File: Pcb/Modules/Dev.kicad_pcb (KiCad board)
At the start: 2 copper layers, 38.1 x 38.1 mm, 9 parts, among them J1 JACK_STEREO, J2 JACK_RJ45, P1 CONN_02X04, P2 CONN_02X04, Q1 BSS138P, U1 11AA160, X1 HOLE, X2 HOLE

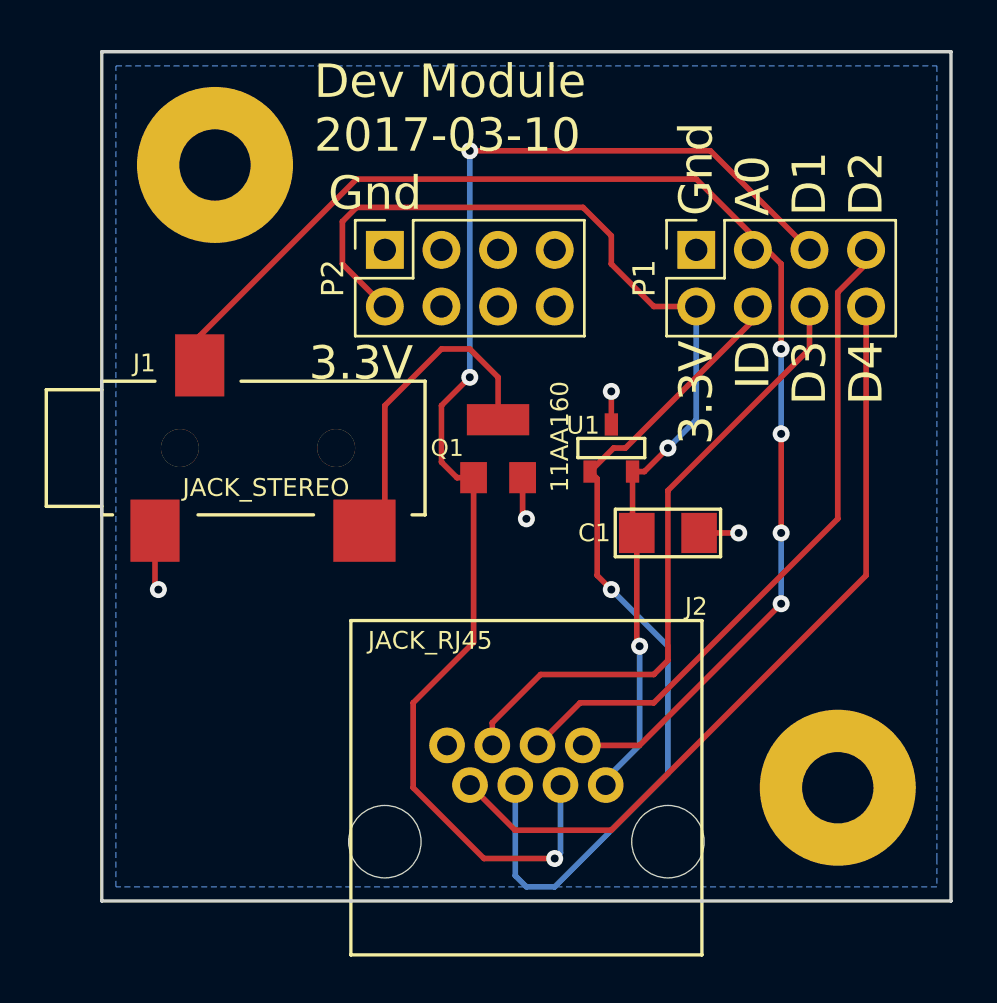
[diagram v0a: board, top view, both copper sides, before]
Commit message: Rework dev board layout so both parts are on same side of the case
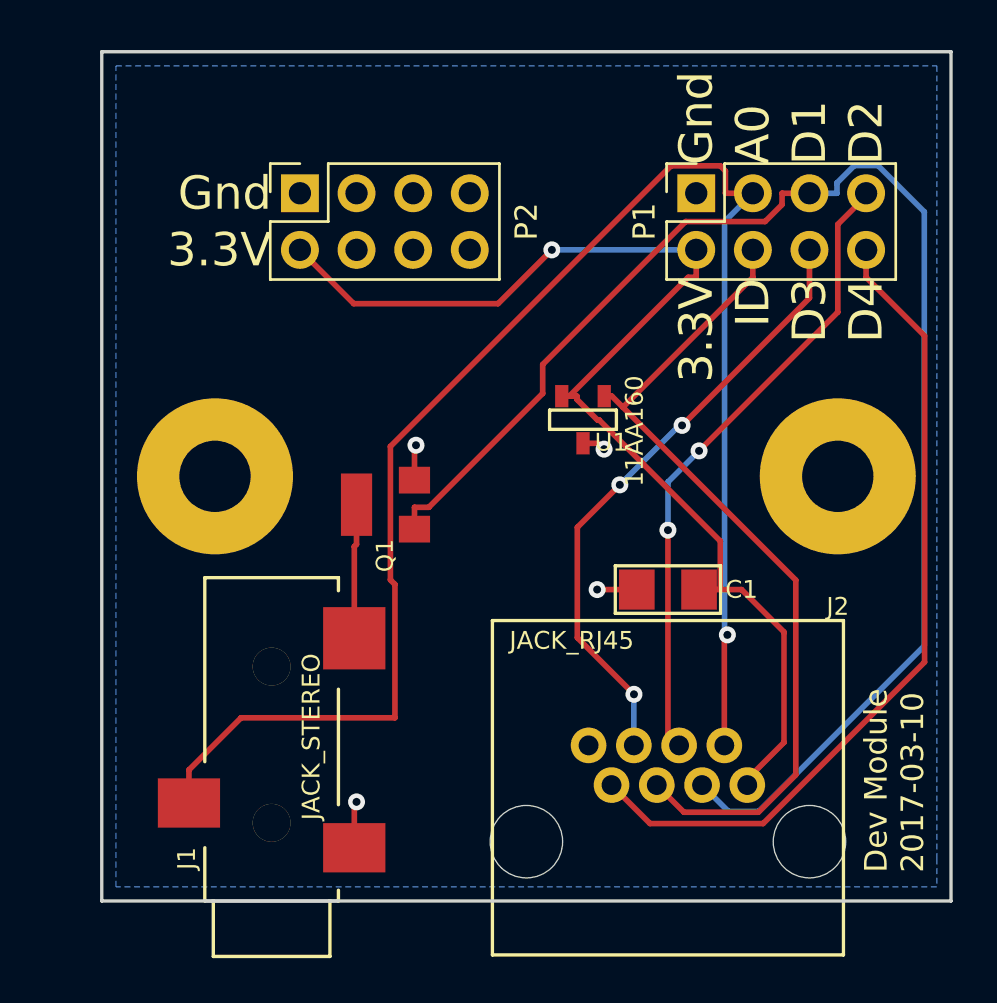
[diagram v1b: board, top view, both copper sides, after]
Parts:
- moved J1 21.7 mm to (33.0, 63.5), turned to 90 degrees
- moved X2 14.0 mm to (30.5, 44.5)
- moved X1 14.0 mm to (58.4, 44.5)
- moved Q1 7.41 mm to (36.8, 45.7), turned to 90 degrees
- moved J2 6.35 mm to (50.8, 58.4)
- moved P2 4.58 mm to (34.3, 31.8)
- moved C1 2.54 mm to (50.8, 49.5), turned to 0 degrees
- moved P1 2.54 mm to (52.1, 31.8)
- moved U1 1.80 mm to (47.0, 41.9), turned to 180 degrees
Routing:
- net /A0: track 59.0 -> 71.9 mm, vias 4 -> 1
- net Net-(J1-Pad2): track 14.6 -> 6.04 mm
- net /D1: track 59.4 -> 65.4 mm, vias 3 -> 0
- net 3V3: track 47.3 -> 53.1 mm, vias 2 -> 1
- net /D4: track 35.4 -> 37.3 mm
- net /D2: track 30.3 -> 28.7 mm, vias 0 -> 2
- net GND: track 7.88 -> 6.53 mm
- net /ID: track 39.0 -> 37.7 mm, vias 1 -> 0
- net /D3: track 28.6 -> 27.7 mm, vias 0 -> 3

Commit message: Give module rounded corners
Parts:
- moved J1 2.54 mm to (35.6, 63.5)
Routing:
- net /A0: track 71.9 -> 51.6 mm, vias 1 -> 2
- net GND: track 6.53 -> 14.3 mm, vias 4 -> 3
- net Net-(J1-Pad2): track 6.04 -> 7.00 mm
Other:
- outline, holes or cut-outs redrawn
- board text added: "Dev Module 2017-04-03"
- board text removed: "Dev Module 2017-03-10"
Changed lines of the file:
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@@
     (links 20)
     (no_connects 0)
-    (area 22.580599 25.324999 63.575001 66.248931)
+    (area 25.324999 25.324999 63.575001 66.319401)
     (thickness 1.6)
-    (drawings 15)
-    (tracks 107)
+    (drawings 19)
+    (tracks 102)
     (zones 0)
     (modules 9)
@@
   )
   (module CA6:161-3334-E_Big_Pad (layer F.Cu)
-    (at 33.02 63.5 90)
+    (at 35.56 63.5 90)
     (fp_text reference J1 (at 1.905 -3.81 90) (layer F.SilkS)
       (effects (font (size 0.8 0.8) (thickness 0.1524)))
@@
     (pad "" np_thru_hole circle (at 0 0) (size 7 7) (drill 3.2) (layers *.Cu *.Mask F.SilkS))
   )
-  (gr_text "Dev Module\n2017-03-10" (at 60.96 62.23 90) (layer F.SilkS)
+  (gr_line (start 25.4 57.15) (end 25.4 31.75) (angle 90) (layer Edge.Cuts) (width 0.15))
+  (gr_line (start 57.15 63.5) (end 31.75 63.5) (angle 90) (layer Edge.Cuts) (width 0.15))
+  (gr_line (start 63.5 31.75) (end 63.5 57.15) (angle 90) (layer Edge.Cuts) (width 0.15))
+  (gr_line (start 31.75 25.4) (end 57.15 25.4) (angle 90) (layer Edge.Cuts) (width 0.15))
+  (gr_arc (start 57.15 57.15) (end 63.5 57.15) (angle 90) (layer Edge.Cuts) (width 0.15))
+  (gr_arc (start 31.75 57.15) (end 31.75 63.5) (angle 90) (layer Edge.Cuts) (width 0.15))
+  (gr_arc (start 31.75 31.75) (end 25.4 31.75) (angle 90) (layer Edge.Cuts) (width 0.15))
+  (gr_arc (start 57.15 31.75) (end 57.15 25.4) (angle 90) (layer Edge.Cuts) (width 0.15))
+  (gr_text "Dev Module\n2017-04-03" (at 60.96 59.055 90) (layer F.SilkS)
     (effects (font (size 1.016 1.016) (thickness 0.1524)) (justify left))
   )
@@
     (effects (font (size 1.5 1.5) (thickness 0.3)) (justify left))
   )
-  (gr_line (start 63.5 63.5) (end 25.4 63.5) (angle 90) (layer Edge.Cuts) (width 0.15))
-  (gr_line (start 25.4 63.5) (end 25.4 25.4) (angle 90) (layer Edge.Cuts) (width 0.15))
-  (gr_line (start 63.5 25.4) (end 63.5 63.5) (angle 90) (layer Edge.Cuts) (width 0.15))
-  (gr_line (start 25.4 25.4) (end 63.5 25.4) (angle 90) (layer Edge.Cuts) (width 0.15))
   (segment (start 52.07 34.29) (end 45.593 34.29) (width 0.254) (layer B.Cu) (net 1))
   (segment (start 36.703 36.703) (end 34.29 34.29) (width 0.254) (layer F.Cu) (net 1))
@@
   (segment (start 46.378 40.8534) (end 51.7101 35.5213) (width 0.254) (layer F.Cu) (net 1))
   (segment (start 52.07 34.29) (end 52.07 35.5213) (width 0.254) (layer F.Cu) (net 1))
-  (segment (start 36.7284 61.1124) (end 36.7284 59.1566) (width 0.254) (layer F.Cu) (net 2))
-  (via (at 36.83 59.055) (size 0.762) (drill 0.3556) (layers F.Cu B.Cu) (net 2))
-  (segment (start 36.7284 59.1566) (end 36.83 59.055) (width 0.254) (layer F.Cu) (net 2))
+  (segment (start 39.2684 61.1124) (end 39.2684 61.0616) (width 0.254) (layer F.Cu) (net 2))
+  (segment (start 39.2684 61.0616) (end 43.81 56.52) (width 0.254) (layer F.Cu) (net 2))
+  (segment (start 43.81 56.52) (end 47.24 56.52) (width 0.254) (layer F.Cu) (net 2))
   (via (at 47.625 49.53) (size 0.762) (layers F.Cu B.Cu) (net 2))
   (via (at 39.497 43.053) (size 0.762) (layers F.Cu B.Cu) (net 2))
@@
   (segment (start 46.99 42.9666) (end 47.671 42.9666) (width 0.254) (layer F.Cu) (net 2))
   (segment (start 47.9354 43.231) (end 47.671 42.9666) (width 0.254) (layer F.Cu) (net 2))
+  (segment (start 31.8516 59.1058) (end 34.2392 59.1058) (width 0.254) (layer F.Cu) (net 3))
+  (segment (start 48.133 51.562) (end 53.467 51.562) (width 0.254) (layer B.Cu) (net 3))
+  (segment (start 47.625 52.07) (end 48.133 51.562) (width 0.254) (layer B.Cu) (net 3))
+  (segment (start 47.625 54.61) (end 47.625 52.07) (width 0.254) (layer B.Cu) (net 3))
+  (via (at 47.625 54.61) (size 0.762) (drill 0.3556) (layers F.Cu B.Cu) (net 3))
+  (segment (start 38.735 54.61) (end 47.625 54.61) (width 0.254) (layer F.Cu) (net 3))
+  (segment (start 34.2392 59.1058) (end 38.735 54.61) (width 0.254) (layer F.Cu) (net 3))
   (segment (start 53.33 56.52) (end 53.33 51.699) (width 0.254) (layer F.Cu) (net 3))
   (segment (start 53.34 33.02) (end 54.61 31.75) (width 0.254) (layer B.Cu) (net 3))
@@
   (via (at 53.467 51.562) (size 0.762) (drill 0.3556) (layers F.Cu B.Cu) (net 3))
   (segment (start 53.33 51.699) (end 53.467 51.562) (width 0.254) (layer F.Cu) (net 3))
-  (segment (start 29.3116 59.1058) (end 29.3116 57.6196) (width 0.254) (layer F.Cu) (net 3))
-  (segment (start 54.61 31.75) (end 53.3787 31.75) (width 0.254) (layer F.Cu) (net 3))
-  (segment (start 38.5514 49.2966) (end 38.5514 55.2821) (width 0.254) (layer F.Cu) (net 3))
-  (segment (start 38.3486 49.0938) (end 38.5514 49.2966) (width 0.254) (layer F.Cu) (net 3))
-  (segment (start 38.3486 43.1086) (end 38.3486 49.0938) (width 0.254) (layer F.Cu) (net 3))
-  (segment (start 50.9386 30.5186) (end 38.3486 43.1086) (width 0.254) (layer F.Cu) (net 3))
-  (segment (start 53.1477 30.5186) (end 50.9386 30.5186) (width 0.254) (layer F.Cu) (net 3))
-  (segment (start 53.3787 30.7496) (end 53.1477 30.5186) (width 0.254) (layer F.Cu) (net 3))
-  (segment (start 53.3787 31.75) (end 53.3787 30.7496) (width 0.254) (layer F.Cu) (net 3))
-  (segment (start 31.6491 55.2821) (end 29.3116 57.6196) (width 0.254) (layer F.Cu) (net 3))
-  (segment (start 38.5514 55.2821) (end 31.6491 55.2821) (width 0.254) (layer F.Cu) (net 3))
-  (segment (start 36.7284 47.6029) (end 36.7284 51.7144) (width 0.254) (layer F.Cu) (net 4))
-  (segment (start 36.83 47.5013) (end 36.7284 47.6029) (width 0.254) (layer F.Cu) (net 4))
-  (segment (start 36.83 45.72) (end 36.83 47.5013) (width 0.254) (layer F.Cu) (net 4))
+  (segment (start 36.83 45.72) (end 36.83 49.276) (width 0.254) (layer F.Cu) (net 4))
+  (segment (start 36.83 49.276) (end 39.2684 51.7144) (width 0.254) (layer F.Cu) (net 4))
   (segment (start 47.9425 40.8534) (end 48.283 40.8534) (width 0.254) (layer F.Cu) (net 5))
   (segment (start 54.61 34.29) (end 54.61 35.5213) (width 0.254) (layer F.Cu) (net 5))
